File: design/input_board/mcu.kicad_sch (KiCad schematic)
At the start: 1 part, among them U16 STM32H753VITx

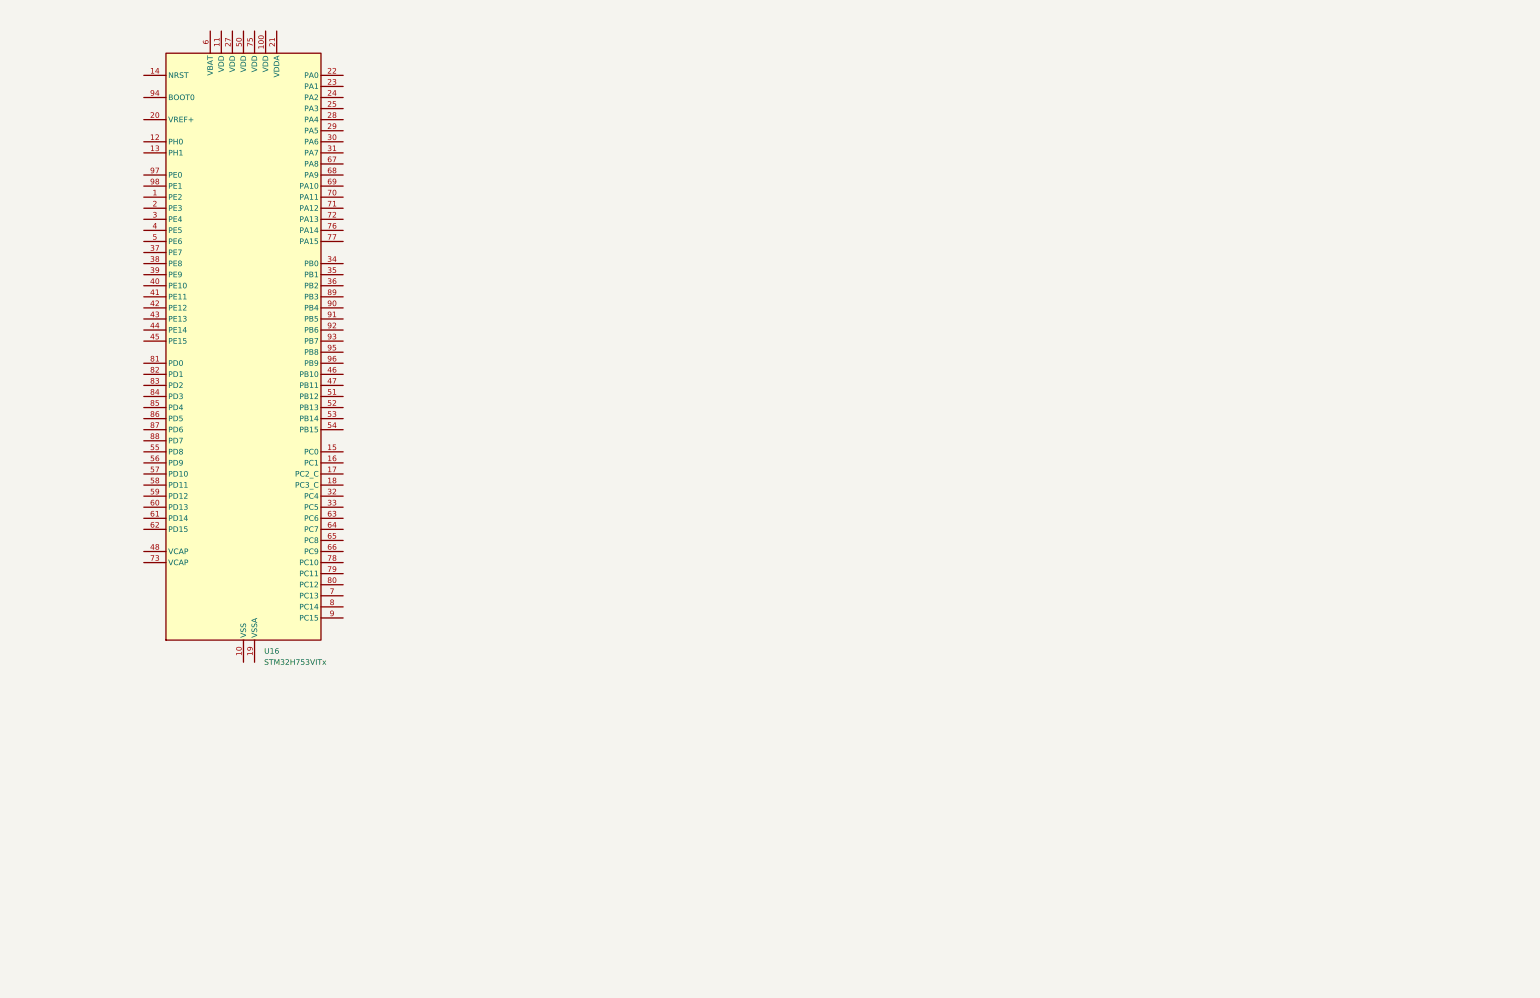
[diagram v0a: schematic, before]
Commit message: Finihs schamtic and footprints; DVDD 3.3->2V
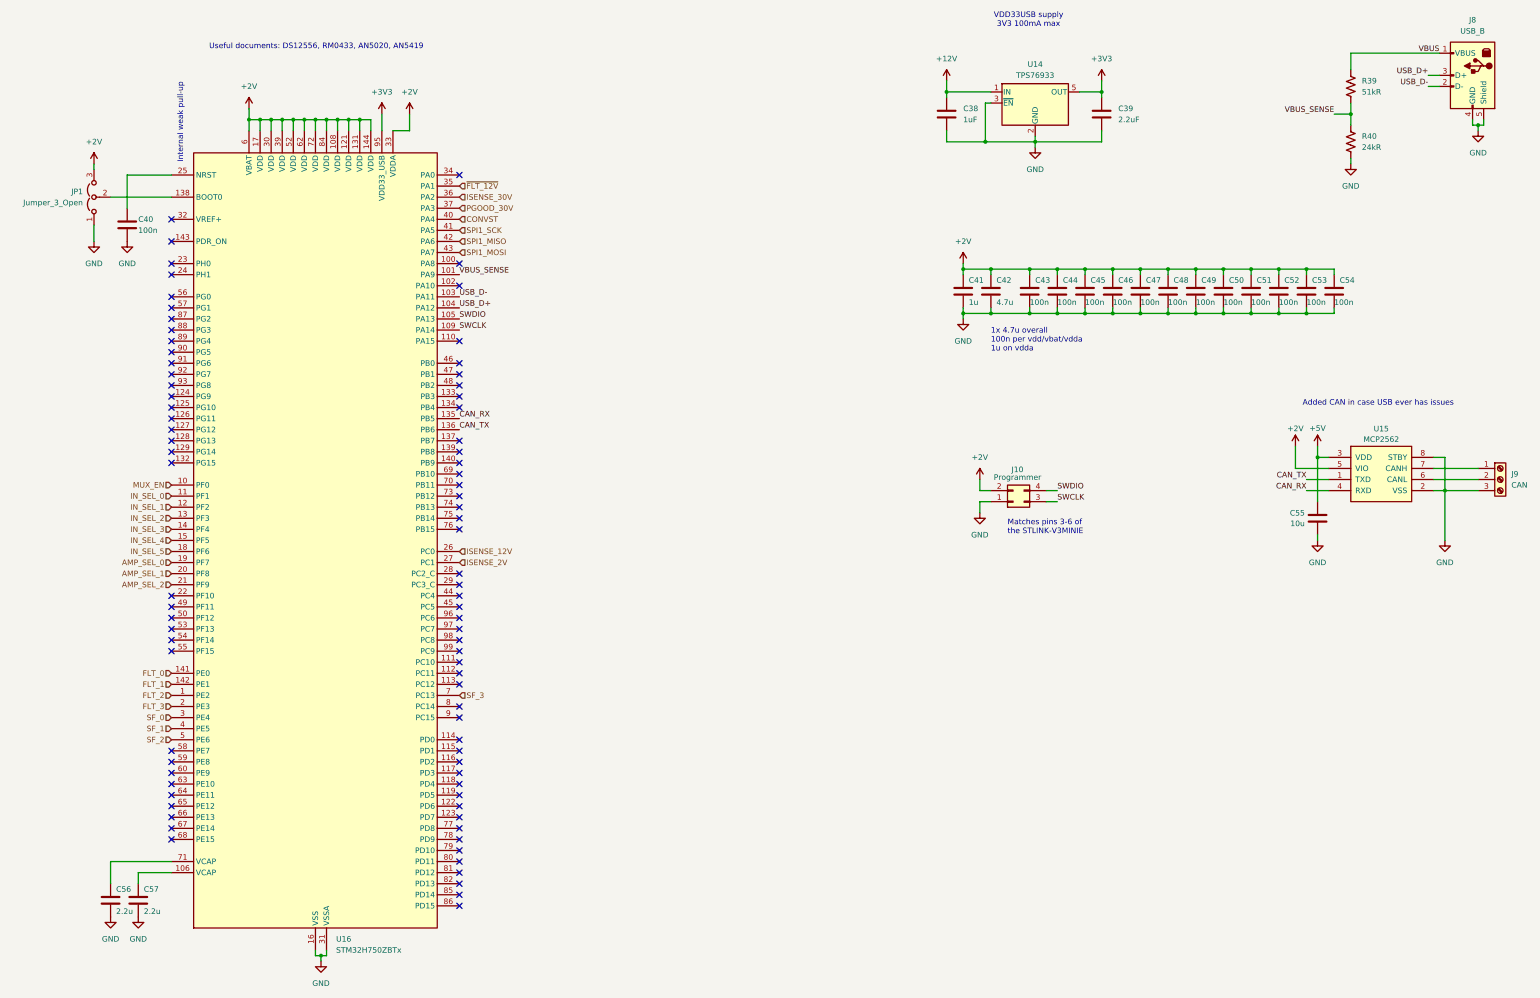
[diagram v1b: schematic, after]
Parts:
- removed U16: STM32H753VITx, Package_QFP:LQFP-100_14x14mm_P0.5mm, symbol MCU_ST_STM32H7:STM32H753VITx
- added C38: 1uF, Capacitor_SMD:C_0805_2012Metric_Pad1.18x1.45mm_HandSolder, symbol Device:C
- added C39: 2.2uF, Capacitor_SMD:C_0805_2012Metric_Pad1.18x1.45mm_HandSolder, symbol Device:C
- added C40, C43, C44, C45, C46, C47, C48, C49, C50, C51, C52, C53, C54: 100n, Capacitor_SMD:C_0805_2012Metric_Pad1.18x1.45mm_HandSolder, symbol Device:C
- added C41: 1u, Capacitor_SMD:C_0805_2012Metric_Pad1.18x1.45mm_HandSolder, symbol Device:C
- added C42: 4.7u, Capacitor_SMD:C_0805_2012Metric_Pad1.18x1.45mm_HandSolder, symbol Device:C
- added C55: 10u, Capacitor_SMD:C_0805_2012Metric_Pad1.18x1.45mm_HandSolder, symbol Device:C
- added C56, C57: 2.2u, Capacitor_SMD:C_0805_2012Metric_Pad1.18x1.45mm_HandSolder, symbol Device:C
- added J10: Programmer, Connector_PinSocket_1.27mm:PinSocket_2x02_P1.27mm_Vertical_SMD, symbol Connector_Generic:Conn_02x02_Top_Bottom
- added J8: USB_B, input_board:CUI_UJ2-BH-1-TH, symbol Connector:USB_B
- added J9: CAN, TerminalBlock_Phoenix:TerminalBlock_Phoenix_MPT-0,5-3-2.54_1x03_P2.54mm_Horizontal, symbol Connector:Screw_Terminal_01x03
- added JP1: Jumper_3_Open, Jumper:SolderJumper-3_P2.0mm_Open_TrianglePad1.0x1.5mm_NumberLabels, symbol Jumper:Jumper_3_Open
- added R39: 51kR, Resistor_SMD:R_0805_2012Metric_Pad1.20x1.40mm_HandSolder, symbol Device:R_US
- added R40: 24kR, Resistor_SMD:R_0805_2012Metric_Pad1.20x1.40mm_HandSolder, symbol Device:R_US
- added U14: TPS76933, Package_TO_SOT_SMD:SOT-23-5, symbol Regulator_Linear:TPS76933
- added U15: MCP2562, Package_SO:SOIC-8_3.9x4.9mm_P1.27mm, symbol canhw:MCP2562
- added U16: STM32H750ZBTx, Package_QFP:LQFP-144_20x20mm_P0.5mm, symbol MCU_ST_STM32H7:STM32H750ZBTx
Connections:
- new net: J9.1 (Pin_1), U15.7 (CANH)
- new net: J9.2 (Pin_2), U15.6 (CANL)
- new net: C56.1, U16.71 (VCAP)
- new net: C40.1, U16.25 (NRST)
- new net: C57.1, U16.106 (VCAP)
- new net: JP1.2 (C), U16.138 (BOOT0)
- new net +12V: C38.1, U14.1 (IN)
- new net +2V: C41.1, C42.1, C43.1, C44.1, C45.1, C46.1, C47.1, C48.1, C49.1, C50.1, C51.1, C52.1, C53.1, C54.1, J10.2 (Pin_2), JP1.3 (B), U15.5 (VIO), U16.108 (VDD), U16.121 (VDD), U16.131 (VDD), U16.144 (VDD), U16.17 (VDD), U16.30 (VDD), U16.33 (VDDA), U16.39 (VDD), U16.52 (VDD), U16.6 (VBAT), U16.62 (VDD), U16.72 (VDD), U16.84 (VDD)
- new net +3V3: C39.1, U14.5 (OUT), U16.95 (VDD33_USB)
- new net +5V: C55.1, U15.3 (VDD)
- new net AMP_SEL_0: U16.19 (PF7)
- new net AMP_SEL_1: U16.20 (PF8)
- new net AMP_SEL_2: U16.21 (PF9)
- new net CAN_RX: U15.4 (RXD), U16.135 (PB5)
- new net CAN_TX: U15.1 (TXD), U16.136 (PB6)
- new net CONVST: U16.40 (PA4)
- new net FLT_0: U16.141 (PE0)
- new net FLT_1: U16.142 (PE1)
- new net FLT_2: U16.1 (PE2)
- new net FLT_3: U16.2 (PE3)
- new net GND: C38.2, C39.2, C40.2, C41.2, C42.2, C43.2, C44.2, C45.2, C46.2, C47.2, C48.2, C49.2, C50.2, C51.2, C52.2, C53.2, C54.2, C55.2, C56.2, C57.2, J10.1 (Pin_1), J8.4 (GND), J8.5 (Shield), J9.3 (Pin_3), JP1.1 (A), R40.2, U14.2 (GND), U14.3 (~{EN}), U15.2 (VSS), U15.8 (STBY), U16.107 (VSS), U16.120 (VSS), U16.130 (VSS), U16.16 (VSS), U16.31 (VSSA), U16.38 (VSS), U16.51 (VSS), U16.61 (VSS), U16.83 (VSS), U16.94 (VSS)
- new net IN_SEL_0: U16.11 (PF1)
- new net IN_SEL_1: U16.12 (PF2)
- new net IN_SEL_2: U16.13 (PF3)
- new net IN_SEL_3: U16.14 (PF4)
- new net IN_SEL_4: U16.15 (PF5)
- new net IN_SEL_5: U16.18 (PF6)
- new net ISENSE_12V: U16.26 (PC0)
- new net ISENSE_2V: U16.27 (PC1)
- new net ISENSE_30V: U16.36 (PA2)
- new net MUX_EN: U16.10 (PF0)
- new net PGOOD_30V: U16.37 (PA3)
- new net SF_0: U16.3 (PE4)
- new net SF_1: U16.4 (PE5)
- new net SF_2: U16.5 (PE6)
- new net SF_3: U16.7 (PC13)
- new net SPI1_MISO: U16.42 (PA6)
- new net SPI1_MOSI: U16.43 (PA7)
- new net SPI1_SCK: U16.41 (PA5)
- new net SWCLK: J10.3 (Pin_3), U16.109 (PA14)
- new net SWDIO: J10.4 (Pin_4), U16.105 (PA13)
- new net USB_D+: J8.3 (D+), U16.104 (PA12)
- new net USB_D-: J8.2 (D-), U16.103 (PA11)
- new net VBUS: J8.1 (VBUS), R39.1
- new net VBUS_SENSE: R39.2, R40.1, U16.101 (PA9)
- new net ~{FLT_12V}: U16.35 (PA1)
- no-connect marks 0 -> 82
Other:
- note added: "1x 4.7u overall 100n per vdd/vbat/vdda 1u on vdda"
- note added: "Added CAN in case USB ever has issues"
- note added: "Internal weak pull-up"
- note added: "Matches pins 3-6 of the STLINK-V3MINIE"
- note added: "Useful documents: DS12556, RM0433, AN5020, AN5419"
- note added: "VDD33USB supply 3V3 100mA max"

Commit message: Layout v2; better
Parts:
- J9: footprint TerminalBlock_Phoenix:TerminalBlock_Phoenix_MPT-0,5-3-2.54_1x03_P2.54mm_Horizontal -> Connector_PinHeader_2.54mm:PinHeader_1x03_P2.54mm_Vertical
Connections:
- net AMP_SEL_0: now also U16.45 (PC5); no longer U16.19 (PF7)
- net AMP_SEL_1: now also U16.47 (PB1); no longer U16.20 (PF8)
- net AMP_SEL_2: now also U16.46 (PB0); no longer U16.21 (PF9)
- net FLT_0: now also U16.76 (PB15); no longer U16.141 (PE0)
- net FLT_1: now also U16.74 (PB13); no longer U16.142 (PE1)
- net FLT_2: now also U16.35 (PA1); no longer U16.1 (PE2)
- net FLT_3: now also U16.28 (PC2_C); no longer U16.2 (PE3)
- net IN_SEL_0: now also U16.22 (PF10); no longer U16.11 (PF1)
- net IN_SEL_1: now also U16.21 (PF9); no longer U16.12 (PF2)
- net IN_SEL_2: now also U16.78 (PD9); no longer U16.13 (PF3)
- net IN_SEL_3: now also U16.79 (PD10); no longer U16.14 (PF4)
- net IN_SEL_4: now also U16.81 (PD12); no longer U16.15 (PF5)
- net IN_SEL_5: now also U16.80 (PD11); no longer U16.18 (PF6)
- net MUX_EN: now also U16.44 (PC4); no longer U16.10 (PF0)
- net SF_0: now also U16.77 (PD8); no longer U16.3 (PE4)
- net SF_1: now also U16.75 (PB14); no longer U16.4 (PE5)
- net SF_2: now also U16.24 (PH1); no longer U16.5 (PE6)
- net SF_3: now also U16.34 (PA0); no longer U16.7 (PC13)
- net ~{FLT_12V}: now also U16.23 (PH0); no longer U16.35 (PA1)
- no-connect marks 82 -> 65
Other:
- moved on the sheet: C40
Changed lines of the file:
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@@
 	)
 	(no_connect
-		(at 142.24 156.21)
-	)
-	(no_connect
 		(at 142.24 199.39)
 	)
@@
 	)
 	(no_connect
-		(at 142.24 143.51)
-	)
-	(no_connect
 		(at 76.2 95.25)
 	)
@@
 	)
 	(no_connect
-		(at 76.2 87.63)
-	)
-	(no_connect
 		(at 76.2 201.93)
 	)
@@
 	)
 	(no_connect
-		(at 142.24 161.29)
-	)
-	(no_connect
 		(at 76.2 214.63)
 	)
 	(no_connect
-		(at 142.24 217.17)
-	)
-	(no_connect
 		(at 76.2 113.03)
 	)
@@
 	)
 	(no_connect
-		(at 142.24 222.25)
-	)
-	(no_connect
 		(at 142.24 173.99)
 	)
 	(no_connect
-		(at 142.24 110.49)
-	)
-	(no_connect
 		(at 142.24 212.09)
 	)
@@
 	)
 	(no_connect
-		(at 142.24 64.77)
-	)
-	(no_connect
 		(at 76.2 217.17)
 	)
 	(no_connect
-		(at 142.24 140.97)
-	)
-	(no_connect
 		(at 76.2 173.99)
 	)
 	(no_connect
-		(at 142.24 219.71)
-	)
-	(no_connect
 		(at 142.24 227.33)
 	)
@@
 	)
 	(no_connect
-		(at 142.24 146.05)
-	)
-	(no_connect
 		(at 76.2 128.27)
 	)
@@
 	)
 	(no_connect
-		(at 76.2 161.29)
-	)
-	(no_connect
 		(at 76.2 100.33)
 	)
@@
 	)
 	(no_connect
-		(at 142.24 214.63)
-	)
-	(no_connect
 		(at 76.2 130.81)
 	)
 	(no_connect
-		(at 76.2 85.09)
-	)
-	(no_connect
 		(at 142.24 209.55)
 	)
@@
 	)
 	(no_connect
-		(at 142.24 163.83)
-	)
-	(no_connect
 		(at 76.2 110.49)
 	)
 	(no_connect
-		(at 142.24 224.79)
-	)
-	(no_connect
 		(at 76.2 209.55)
 	)
 	(no_connect
-		(at 142.24 107.95)
-	)
-	(no_connect
 		(at 76.2 115.57)
 	)
@@
 	(wire
 		(pts
-			(xy 66.04 64.77) (xy 66.04 72.39)
+			(xy 64.77 64.77) (xy 64.77 72.39)
 		)
 		(stroke
@@
 	(wire
 		(pts
-			(xy 66.04 64.77) (xy 76.2 64.77)
+			(xy 64.77 64.77) (xy 76.2 64.77)
 		)
 		(stroke
@@
 	(hierarchical_label "AMP_SEL_2"
 		(shape input)
-		(at 76.2 158.75 180)
+		(at 142.24 107.95 0)
 		(effects
 			(font
 				(size 1.27 1.27)
 			)
-			(justify right)
+			(justify left)
 		)
 	)
 	(hierarchical_label "IN_SEL_2"
 		(shape input)
-		(at 76.2 143.51 180)
+		(at 142.24 217.17 0)
 		(effects
 			(font
 				(size 1.27 1.27)
 			)
-			(justify right)
+			(justify left)
 		)
 	)
@@
 	(hierarchical_label "FLT_1"
 		(shape input)
-		(at 76.2 181.61 180)
+		(at 142.24 140.97 0)
 		(effects
 			(font
 				(size 1.27 1.27)
 			)
-			(justify right)
+			(justify left)
 		)
 	)
 	(hierarchical_label "AMP_SEL_0"
 		(shape input)
-		(at 76.2 153.67 180)
+		(at 142.24 163.83 0)
 		(effects
 			(font
 				(size 1.27 1.27)
 			)
-			(justify right)
+			(justify left)
 		)
 	)
 	(hierarchical_label "SF_0"
 		(shape input)
-		(at 76.2 189.23 180)
+		(at 142.24 214.63 0)
 		(effects
 			(font
 				(size 1.27 1.27)
 			)
-			(justify right)
+			(justify left)
 		)
 	)
 	(hierarchical_label "SF_3"
 		(shape input)
-		(at 142.24 184.15 0)
+		(at 142.24 64.77 0)
 		(effects
 			(font
@@
 	(hierarchical_label "FLT_3"
 		(shape input)
-		(at 76.2 186.69 180)
+		(at 142.24 156.21 0)
 		(effects
 			(font
 				(size 1.27 1.27)
 			)
-			(justify right)
+			(justify left)
 		)
 	)
 	(hierarchical_label "IN_SEL_0"
 		(shape input)
-		(at 76.2 138.43 180)
+		(at 76.2 161.29 180)
 		(effects
 			(font
@@
 	(hierarchical_label "SF_1"
 		(shape input)
-		(at 76.2 191.77 180)
+		(at 142.24 143.51 0)
 		(effects
 			(font
 				(size 1.27 1.27)
 			)
-			(justify right)
+			(justify left)
 		)
 	)
@@
 	(hierarchical_label "IN_SEL_4"
 		(shape input)
-		(at 76.2 148.59 180)
+		(at 142.24 224.79 0)
 		(effects
 			(font
 				(size 1.27 1.27)
 			)
-			(justify right)
+			(justify left)
 		)
 	)
 	(hierarchical_label "SF_2"
 		(shape input)
-		(at 76.2 194.31 180)
+		(at 76.2 87.63 180)
 		(effects
 			(font
@@
 	(hierarchical_label "IN_SEL_5"
 		(shape input)
-		(at 76.2 151.13 180)
+		(at 142.24 222.25 0)
 		(effects
 			(font
 				(size 1.27 1.27)
 			)
-			(justify right)
+			(justify left)
 		)
 	)
 	(hierarchical_label "IN_SEL_1"
 		(shape input)
-		(at 76.2 140.97 180)
+		(at 76.2 158.75 180)
 		(effects
 			(font
@@
 	(hierarchical_label "FLT_0"
 		(shape input)
-		(at 76.2 179.07 180)
+		(at 142.24 146.05 0)
 		(effects
 			(font
 				(size 1.27 1.27)
 			)
-			(justify right)
+			(justify left)
 		)
 	)
@@
 	(hierarchical_label "~{FLT_12V}"
 		(shape input)
-		(at 142.24 67.31 0)
+		(at 76.2 85.09 180)
 		(effects
 			(font
 				(size 1.27 1.27)
 			)
-			(justify left)
+			(justify right)
 		)
 	)
@@
 	(hierarchical_label "FLT_2"
 		(shape input)
-		(at 76.2 184.15 180)
+		(at 142.24 67.31 0)
 		(effects
 			(font
 				(size 1.27 1.27)
 			)
-			(justify right)
+			(justify left)
 		)
 	)
 	(hierarchical_label "MUX_EN"
 		(shape input)
-		(at 76.2 135.89 180)
+		(at 142.24 161.29 0)
 		(effects
 			(font
 				(size 1.27 1.27)
 			)
-			(justify right)
+			(justify left)
 		)
 	)
 	(hierarchical_label "IN_SEL_3"
 		(shape input)
-		(at 76.2 146.05 180)
+		(at 142.24 219.71 0)
 		(effects
 			(font
 				(size 1.27 1.27)
 			)
-			(justify right)
+			(justify left)
 		)
 	)
 	(hierarchical_label "AMP_SEL_1"
 		(shape input)
-		(at 76.2 156.21 180)
+		(at 142.24 110.49 0)
 		(effects
 			(font
 				(size 1.27 1.27)
 			)
-			(justify right)
+			(justify left)
 		)
 	)
@@
 			)
 		)
-		(property "Footprint" "TerminalBlock_Phoenix:TerminalBlock_Phoenix_MPT-0,5-3-2.54_1x03_P2.54mm_Horizontal"
+		(property "Footprint" "Connector_PinHeader_2.54mm:PinHeader_1x03_P2.54mm_Vertical"
 			(at 381 134.62 0)
 			(effects
@@
 	(symbol
 		(lib_id "Device:C")
-		(at 66.04 76.2 0)
+		(at 64.77 76.2 0)
 		(unit 1)
 		(exclude_from_sim no)
@@
 		(dnp no)
 		(property "Reference" "C40"
-			(at 68.58 74.93 0)
+			(at 67.31 74.93 0)
 			(effects
 				(font
@@
 		)
 		(property "Value" "100n"
-			(at 68.58 77.47 0)
+			(at 67.31 77.47 0)
 			(effects
 				(font
@@
 		)
 		(property "Footprint" "Capacitor_SMD:C_0805_2012Metric_Pad1.18x1.45mm_HandSolder"
-			(at 67.0052 80.01 0)
+			(at 65.7352 80.01 0)
 			(effects
 				(font
@@
 		)
 		(property "Datasheet" "~"
-			(at 66.04 76.2 0)
+			(at 64.77 76.2 0)
 			(effects
 				(font
@@
 		)
 		(property "Description" ""
-			(at 66.04 76.2 0)
+			(at 64.77 76.2 0)
 			(effects
 				(font
@@
 	(symbol
 		(lib_id "power:GND")
-		(at 66.04 80.01 0)
+		(at 64.77 80.01 0)
 		(unit 1)
 		(exclude_from_sim no)
@@
 		(fields_autoplaced yes)
 		(property "Reference" "#PWR0121"
-			(at 66.04 86.36 0)
+			(at 64.77 86.36 0)
 			(effects
 				(font
@@
 		)
 		(property "Value" "GND"
-			(at 66.04 85.09 0)
+			(at 64.77 85.09 0)
 			(effects
 				(font
@@
 		)
 		(property "Footprint" ""
-			(at 66.04 80.01 0)
+			(at 64.77 80.01 0)
 			(effects
 				(font
@@
 		)
 		(property "Datasheet" ""
-			(at 66.04 80.01 0)
+			(at 64.77 80.01 0)
 			(effects
 				(font
@@
 		)
 		(property "Description" "Power symbol creates a global label with name \"GND\" , ground"
-			(at 66.04 80.01 0)
+			(at 64.77 80.01 0)
 			(effects
 				(font
